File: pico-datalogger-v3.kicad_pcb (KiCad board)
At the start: 2 copper layers, 130 x 65 mm, 60 parts, among them IC1 LM66200DRLR, J1 JST-PH2 Bat, J11 Conn_I2C1, J12 Conn_UART_5V, J13 THT_I2C1, J14 THT_I2C0, J17 Disp_THT, J2 Conn_Pico_Left, J3 Conn_Pico_Right, J4 SM06B-GHS-TB_LF_SN, J6 Conn_Display, J9 Conn_I2C0, Q1 AO3401A, Q2 AO3401A, SW1 SW_Push, SW2 SW_Push, SW3 SW_Push, SW4 SW_Push, SW5 SW_Push, U1 74LVC2G74, U2 PCF8523T, U4 XTSD, U5 SCD40_Breakout, U6 AHT20, U7 RFM95W-868S2, Y1 Crystal

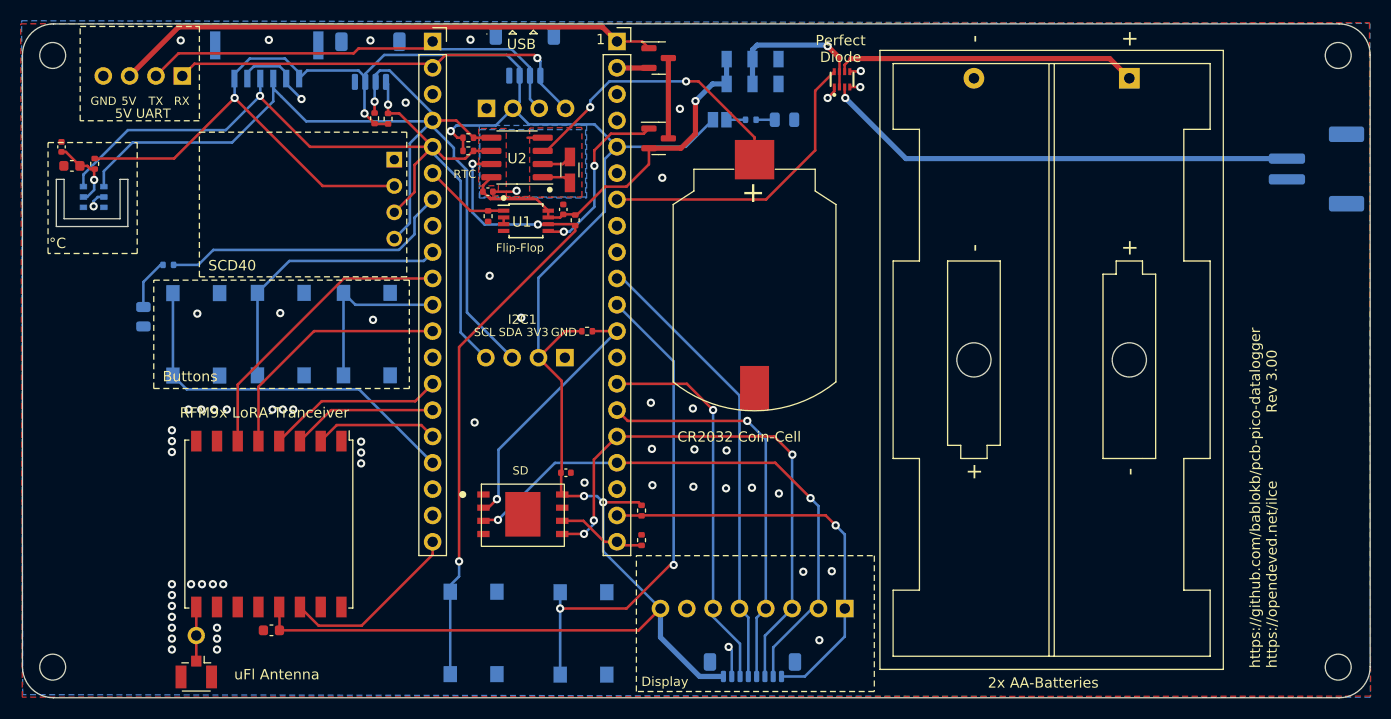
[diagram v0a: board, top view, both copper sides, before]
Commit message: updated production-files for datalogger-v3 and images
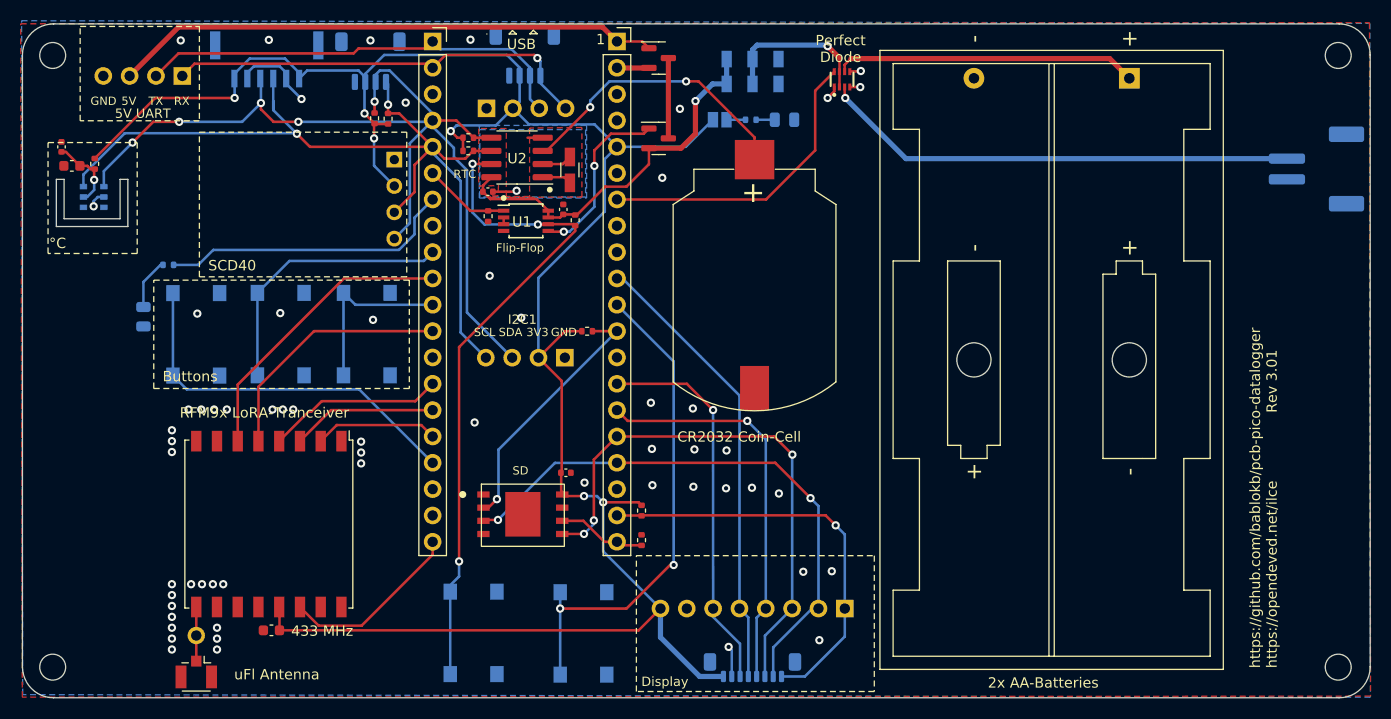
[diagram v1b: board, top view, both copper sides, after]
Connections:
- J4 pad 3: SCL -> SDA
- J4 pad 4: SDA -> SCL
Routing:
- net +3V3: track 224.7 -> 212.6 mm, vias 5 -> 6
- net SCL: track 87.3 -> 89.5 mm
- net SDA: track 96.7 -> 96.6 mm, vias 1 -> 5
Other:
- board text added: "433 MHz"
- board text added: "https://github.com/bablokb/pcb-pico-datalogger https://opendeved.net/ilce Rev 3.01"
- board text removed: "https://github.com/bablokb/pcb-pico-datalogger https://opendeved.net/ilce Rev 3.00"

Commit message: updated production-files for datalogger-v3 (with rfm95-868)
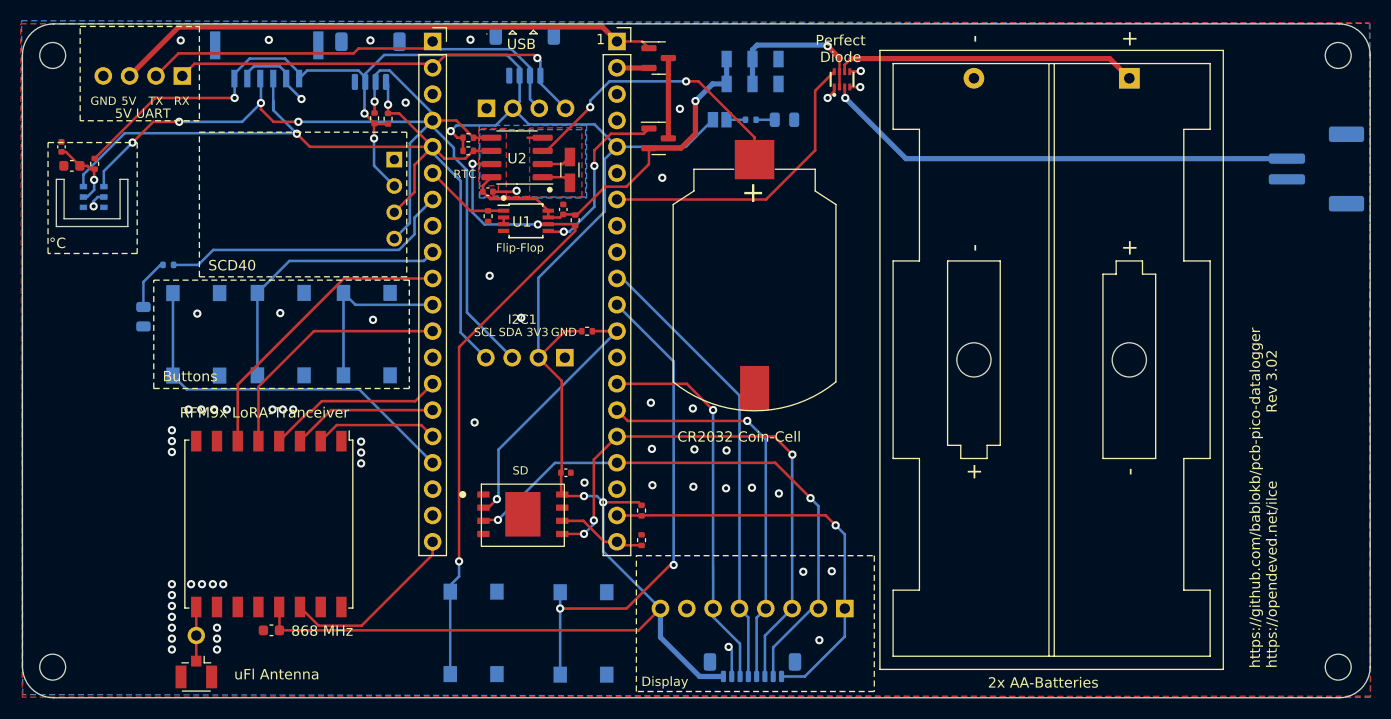
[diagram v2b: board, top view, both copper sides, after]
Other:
- board text added: "868 MHz"
- board text added: "https://github.com/bablokb/pcb-pico-datalogger https://opendeved.net/ilce Rev 3.02"
- board text removed: "433 MHz"
- board text removed: "https://github.com/bablokb/pcb-pico-datalogger https://opendeved.net/ilce Rev 3.01"
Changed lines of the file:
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@@
     (descr "Low Power Long Range Transceiver Module SMD-16 (https://www.hoperf.com/data/upload/portal/20181127/5bfcbea20e9ef.pdf)")
     (tags "LoRa Low Power Long Range Transceiver Module")
-    (property "LCSC" "C2844474")
+    (property "LCSC" "C2844472")
     (property "Sheetfile" "lora.kicad_sch")
     (property "Sheetname" "LoRa")
@@
     (effects (font (size 1 1) (thickness 0.15)) (justify left bottom))
   )
-  (gr_text "https://github.com/bablokb/pcb-pico-datalogger\nhttps://opendeved.net/ilce               Rev 3.01" (at 219.8 162.1 90) (layer "F.SilkS")
+  (gr_text "https://github.com/bablokb/pcb-pico-datalogger\nhttps://opendeved.net/ilce               Rev 3.02" (at 219.8 162.1 90) (layer "F.SilkS")
     (effects (font (size 1 1) (thickness 0.15)) (justify left))
   )
-  (gr_text "433 MHz" (at 126 159.1) (layer "F.SilkS")
+  (gr_text "868 MHz" (at 126 159.1) (layer "F.SilkS")
     (effects (font (size 1 1) (thickness 0.15)) (justify left bottom))
   )

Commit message: Rev. 3.10: use XSON-8 package for flip-flop
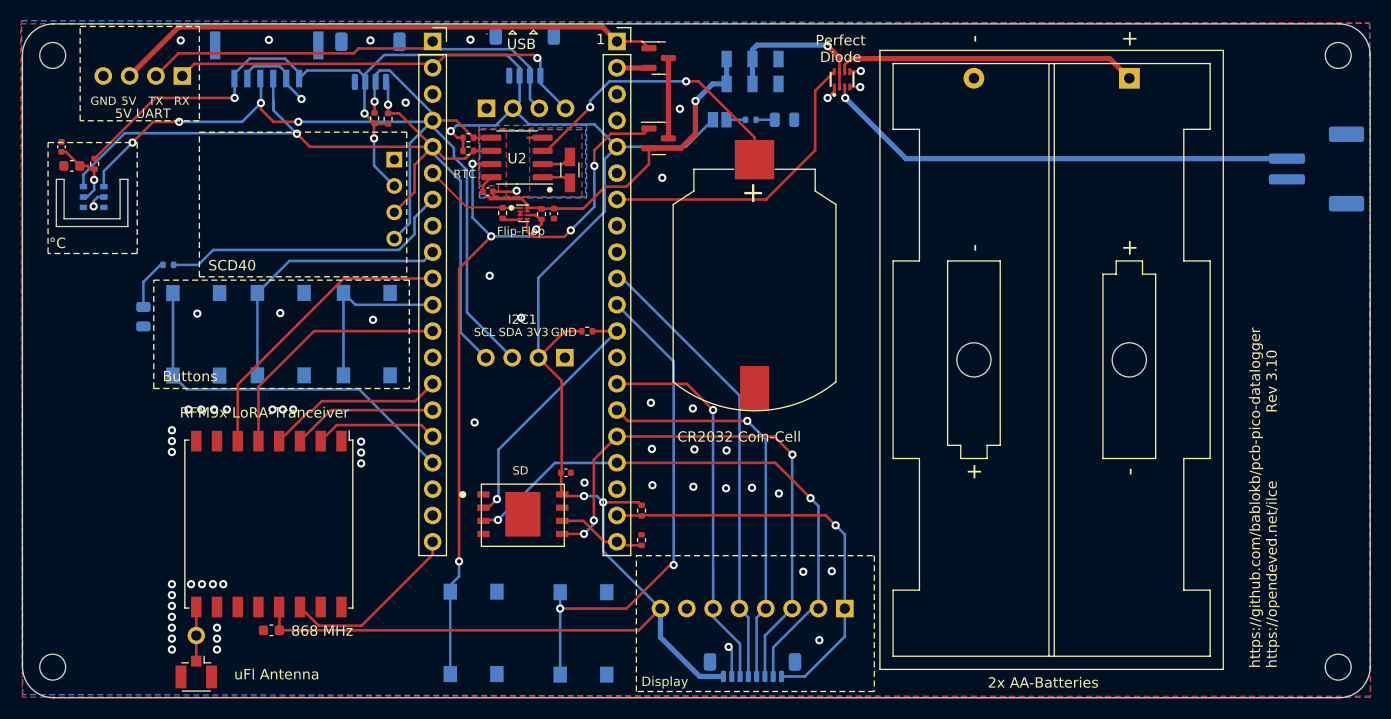
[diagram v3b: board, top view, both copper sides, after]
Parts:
- U1: footprint Package_SO:TSSOP-8_3x3mm_P0.65mm -> Package_SON:X2SON-8_1.4x1mm_P0.35mm
- moved R2 3.30 mm to (150.2, 118.3)
- moved R1 1.43 mm to (146.4, 118.2)
- moved C1 0.98 mm to (151.3, 118.2), turned to -90 degrees
- moved U1 0.76 mm to (148.4, 118.2)
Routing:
- net ~{ON}: track 65.2 -> 60.6 mm, vias 3 -> 4
- net /PC_GATE: track 17.1 -> 20.6 mm
- net GND: track 19.8 -> 21.5 mm
- net /GP4_DONE: track 8.27 -> 9.83 mm
- net +BATT: track 37.1 -> 36.6 mm
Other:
- board text added: "https://github.com/bablokb/pcb-pico-datalogger https://opendeved.net/ilce Rev 3.10"
- board text removed: "https://github.com/bablokb/pcb-pico-datalogger https://opendeved.net/ilce Rev 3.02"
